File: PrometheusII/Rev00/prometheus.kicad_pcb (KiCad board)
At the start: 4 copper layers, 153.2 x 128.5 mm, 181 parts, among them J1 0878311420, J2 Conn_02x08_Odd_Even, Q1 MMBF4391, Q2 MMBF4391, Q3 BSS138, Q4 BSS84, Q5 BSS138, Q6 BSS84, U1 Teensy4.0_NoSD, U10 74LVC2G157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

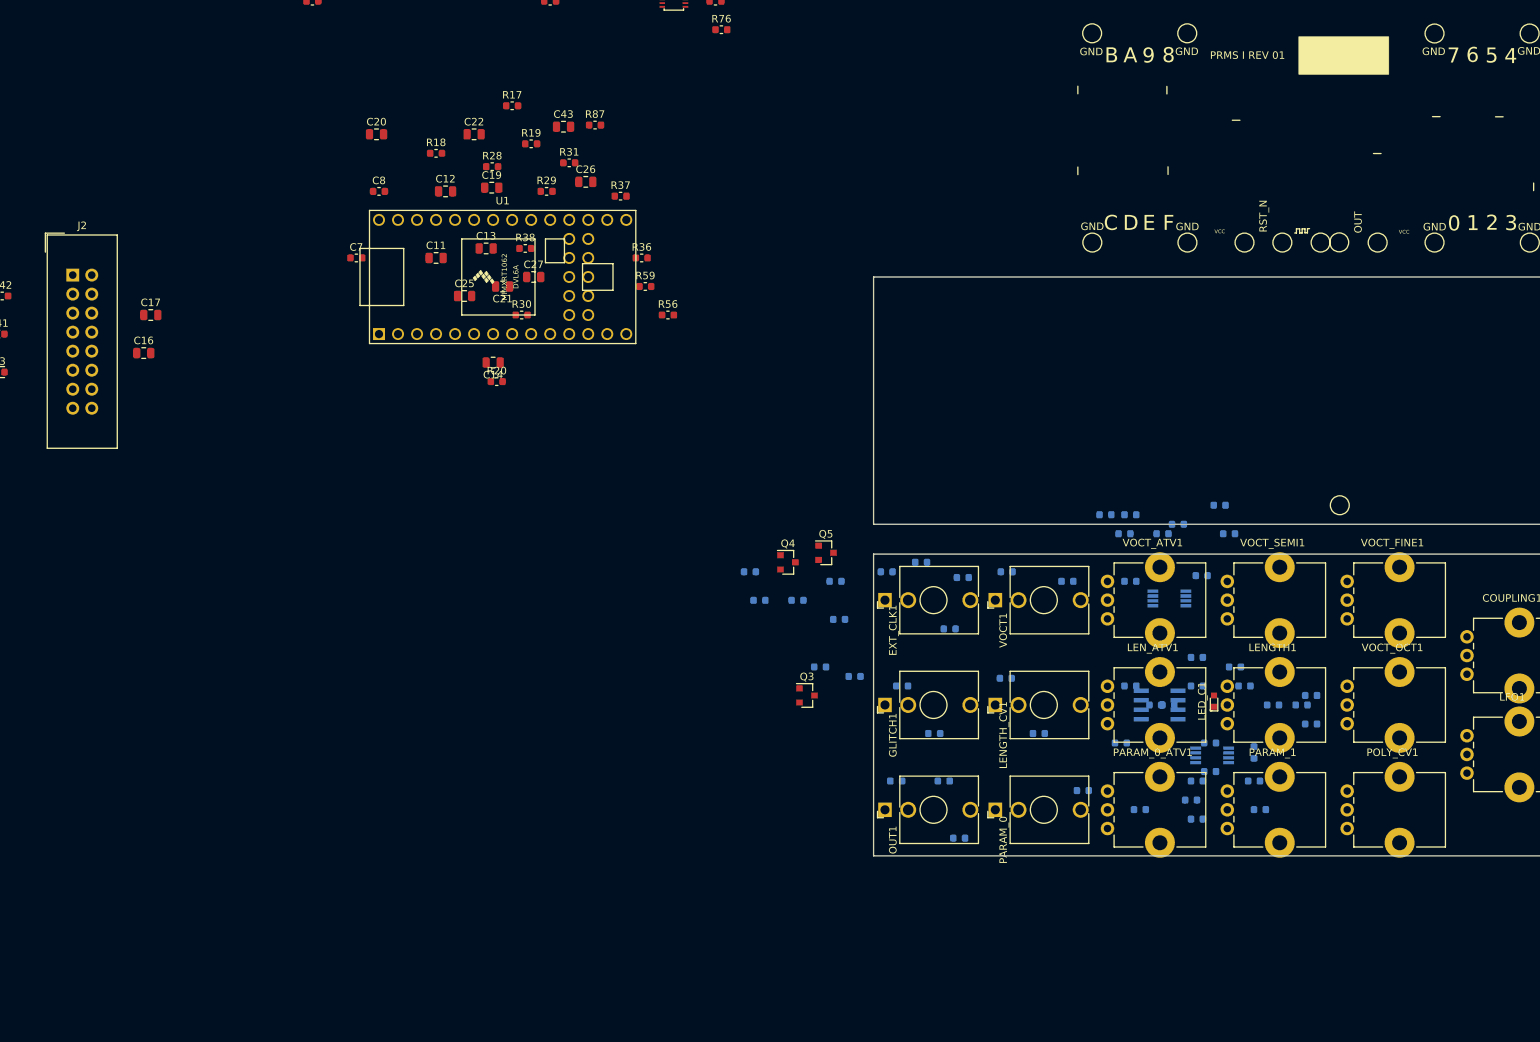
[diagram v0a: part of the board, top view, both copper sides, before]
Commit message: Updated panel layout
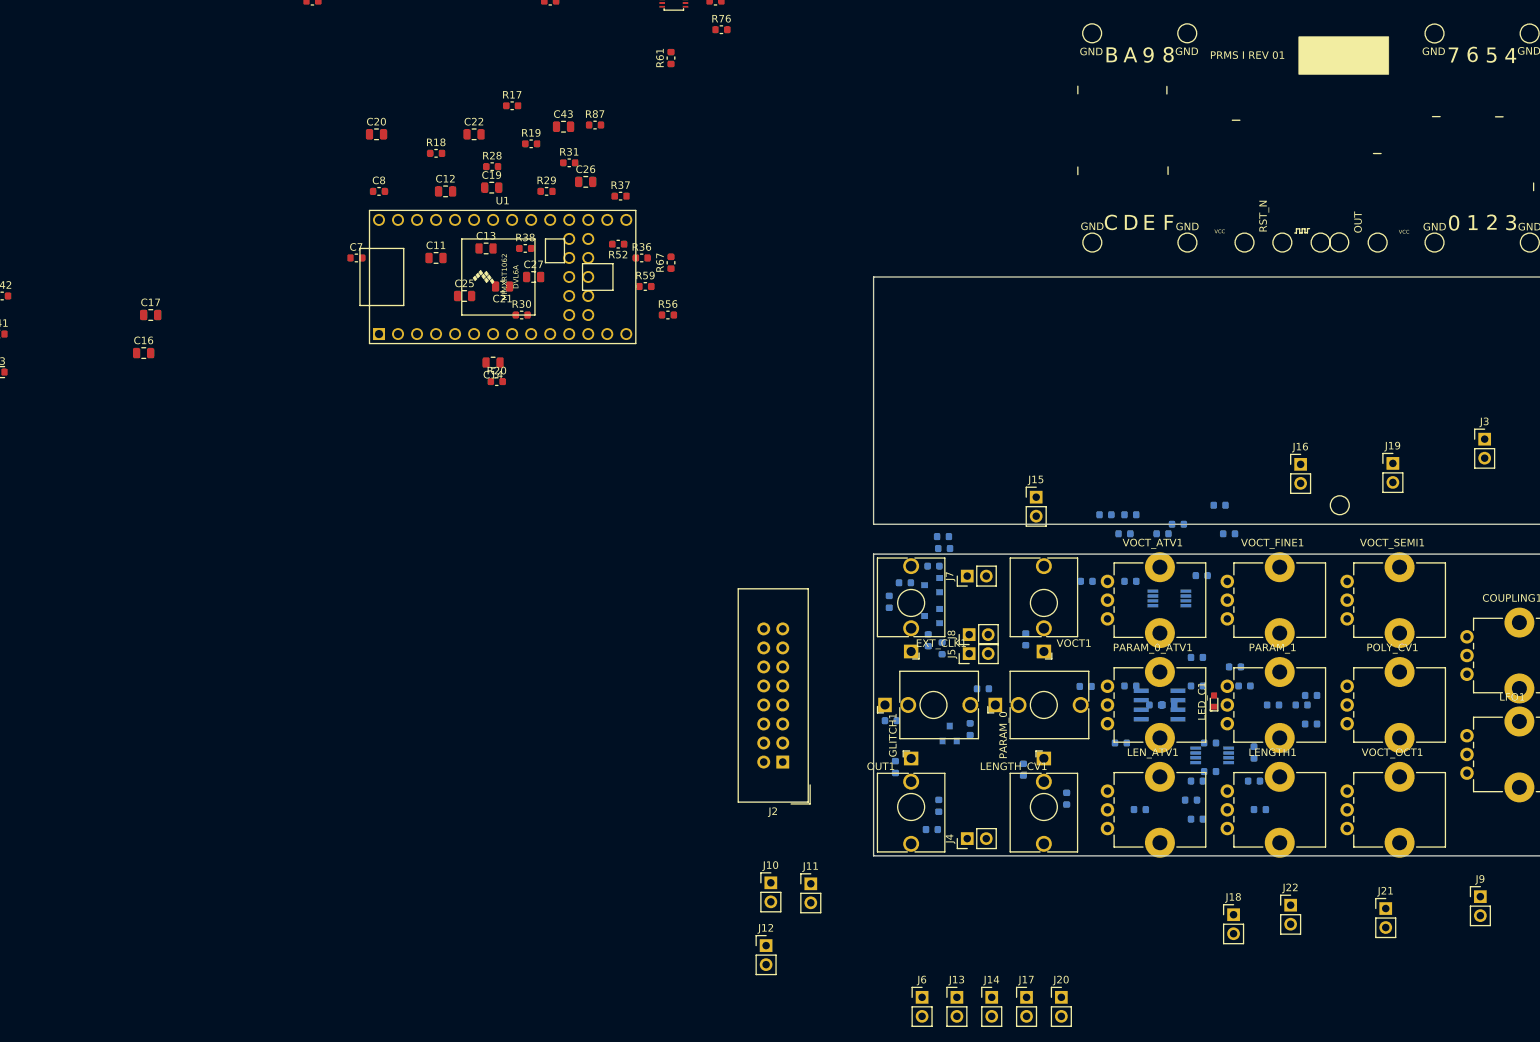
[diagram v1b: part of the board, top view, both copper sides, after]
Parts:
- added J10: Conn_02x01, Connector_PinHeader_2.54mm:PinHeader_1x02_P2.54mm_Vertical, F.Cu at (2.79, 133.0)
- added J11: Conn_02x01, Connector_PinHeader_2.54mm:PinHeader_1x02_P2.54mm_Vertical, F.Cu at (8.13, 133.1)
- added J12: Conn_02x01, Connector_PinHeader_2.54mm:PinHeader_1x02_P2.54mm_Vertical, F.Cu at (2.16, 141.4)
- added J13: Conn_02x01, Connector_PinHeader_2.54mm:PinHeader_1x02_P2.54mm_Vertical, F.Cu at (27.6, 148.3)
- added J14: Conn_02x01, Connector_PinHeader_2.54mm:PinHeader_1x02_P2.54mm_Vertical, F.Cu at (32.3, 148.3)
- added J15: Conn_02x01, Connector_PinHeader_2.54mm:PinHeader_1x02_P2.54mm_Vertical, F.Cu at (38.2, 81.5)
- added J16: Conn_02x01, Connector_PinHeader_2.54mm:PinHeader_1x02_P2.54mm_Vertical, F.Cu at (73.5, 77.1)
- added J17: Conn_02x01, Connector_PinHeader_2.54mm:PinHeader_1x02_P2.54mm_Vertical, F.Cu at (36.9, 148.3)
- added J18: Conn_02x01, Connector_PinHeader_2.54mm:PinHeader_1x02_P2.54mm_Vertical, F.Cu at (64.6, 137.2)
- added J19: Conn_02x01, Connector_PinHeader_2.54mm:PinHeader_1x02_P2.54mm_Vertical, F.Cu at (85.9, 77.0)
- added J20: Conn_02x01, Connector_PinHeader_2.54mm:PinHeader_1x02_P2.54mm_Vertical, F.Cu at (41.6, 148.3)
- added J21: Conn_02x01, Connector_PinHeader_2.54mm:PinHeader_1x02_P2.54mm_Vertical, F.Cu at (84.9, 136.4)
- added J22: Conn_02x01, Connector_PinHeader_2.54mm:PinHeader_1x02_P2.54mm_Vertical, F.Cu at (72.2, 136.0)
- added J3: Conn_02x01, Connector_PinHeader_2.54mm:PinHeader_1x02_P2.54mm_Vertical, F.Cu at (98.1, 73.7)
- added J4: Conn_02x01, Connector_PinHeader_2.54mm:PinHeader_1x02_P2.54mm_Vertical, F.Cu at (29.0, 127.1)
- added J5: Conn_02x01, Connector_PinHeader_2.54mm:PinHeader_1x02_P2.54mm_Vertical, F.Cu at (29.3, 102.4)
- added J6: Conn_02x01, Connector_PinHeader_2.54mm:PinHeader_1x02_P2.54mm_Vertical, F.Cu at (23.0, 148.3)
- added J7: Conn_02x01, Connector_PinHeader_2.54mm:PinHeader_1x02_P2.54mm_Vertical, F.Cu at (29.0, 92.0)
- added J8: Conn_02x01, Connector_PinHeader_2.54mm:PinHeader_1x02_P2.54mm_Vertical, F.Cu at (29.3, 99.8)
- added J9: Conn_02x01, Connector_PinHeader_2.54mm:PinHeader_1x02_P2.54mm_Vertical, F.Cu at (97.5, 134.8)
- Q3, Q4, Q5: moved to B.Cu
- R52, R61, R67: moved to F.Cu
- moved J2 115.0 mm to (4.38, 116.8), turned to 180 degrees
- moved R61 74.4 mm to (-10.5, 22.8), turned to 90 degrees
- moved R52 65.8 mm to (-17.6, 47.7), turned to 180 degrees
- moved R67 52.7 mm to (-10.5, 50.2), turned to 90 degrees
- moved R69 26.2 mm to (25.8, 86.7), turned to 180 degrees
- moved R68 25.6 mm to (25.9, 88.3), turned to 180 degrees
- moved R50 21.7 mm to (29.4, 112.5), turned to 90 degrees
- moved Q4 20.5 mm to (24.3, 97.3), turned to 180 degrees
- moved Q3 19.7 mm to (26.7, 113.0), turned to 90 degrees
- moved VOCT_FINE1 16.0 mm to (63.7, 97.7)
- moved VOCT_SEMI1 16.0 mm to (79.8, 97.7)
- moved Q5 14.8 mm to (24.3, 93.2), turned to 180 degrees
- moved LENGTH1 14.0 mm to (63.7, 125.7)
- moved LEN_ATV1 14.0 mm to (47.7, 125.7)
- moved PARAM_0 14.0 mm to (32.8, 109.2)
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
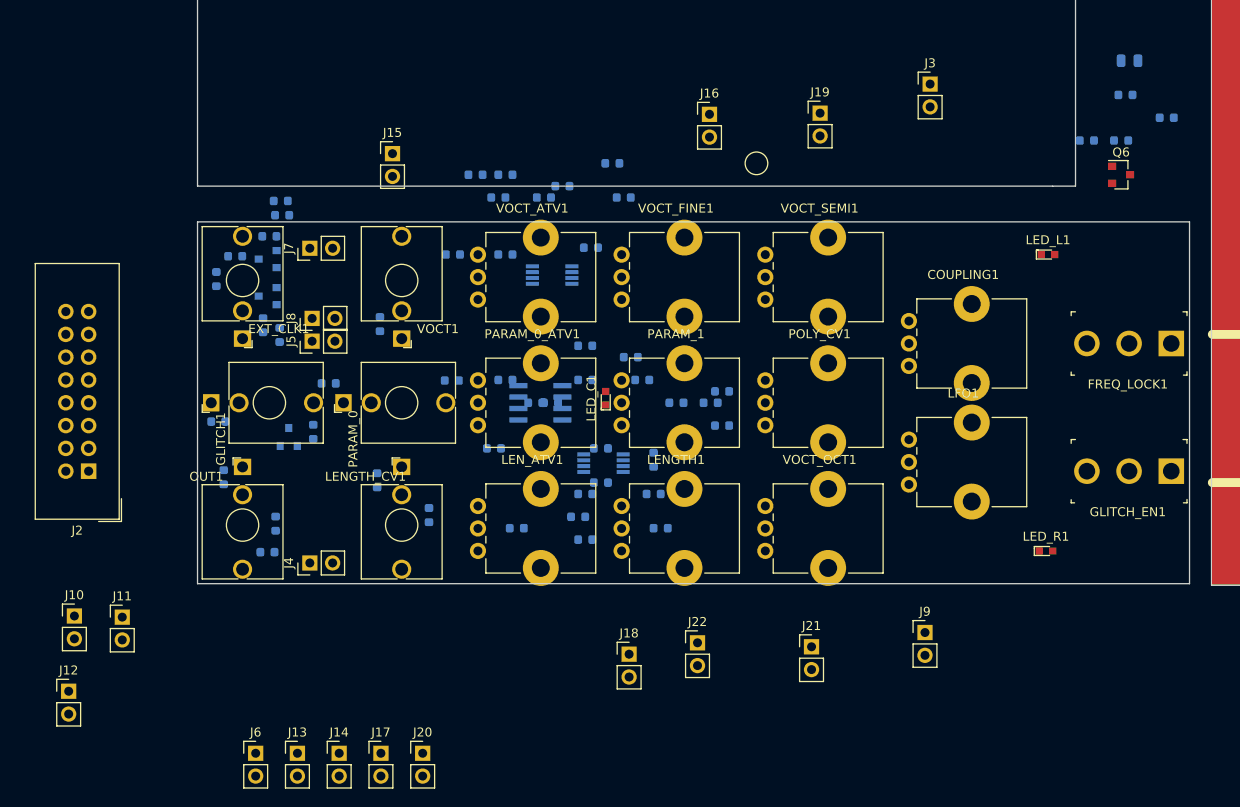
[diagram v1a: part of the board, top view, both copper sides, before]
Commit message: rough board to board connector placement
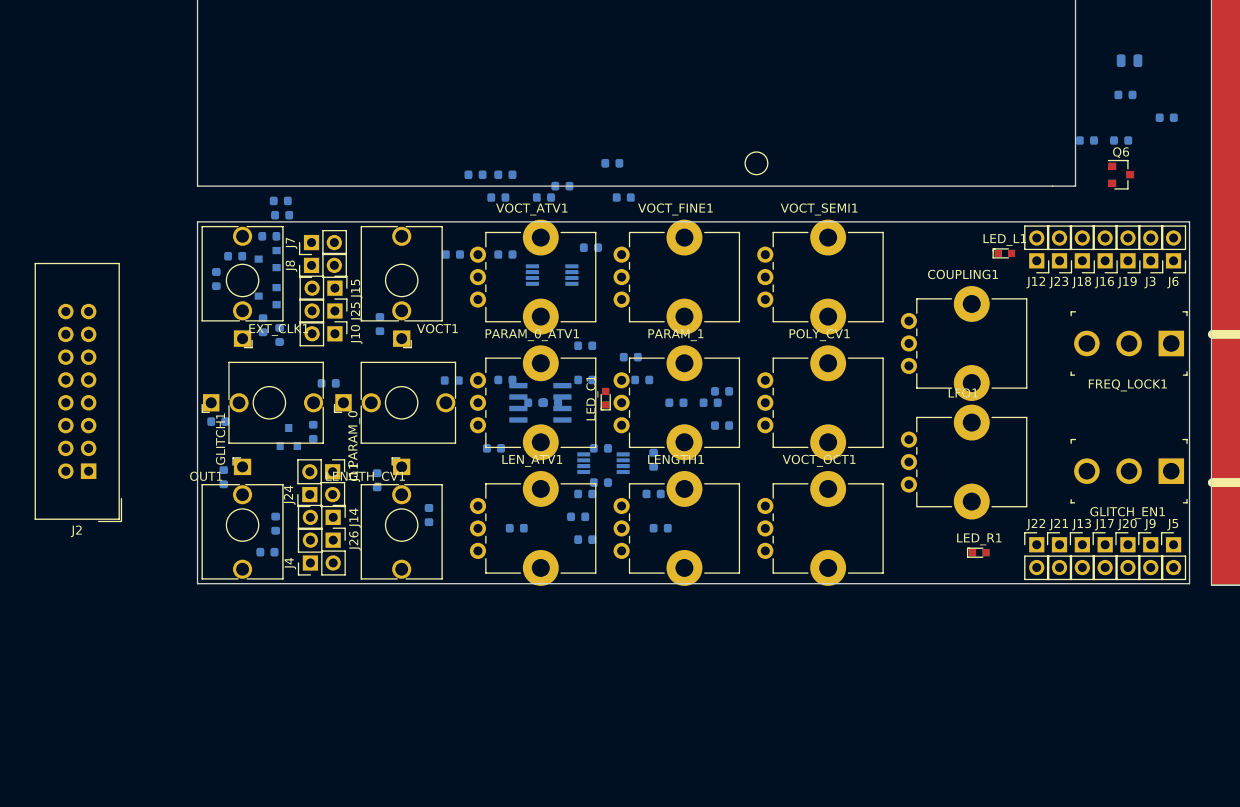
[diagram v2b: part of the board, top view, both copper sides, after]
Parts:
- added J23: Conn_02x01, Connector_PinHeader_2.54mm:PinHeader_1x02_P2.54mm_Vertical, F.Cu at (112.5, 93.4)
- added J24: Conn_02x01, Connector_PinHeader_2.54mm:PinHeader_1x02_P2.54mm_Vertical, F.Cu at (29.0, 119.4)
- added J25: Conn_02x01, Connector_PinHeader_2.54mm:PinHeader_1x02_P2.54mm_Vertical, F.Cu at (31.8, 99.0)
- added J26: Conn_02x01, Connector_PinHeader_2.54mm:PinHeader_1x02_P2.54mm_Vertical, F.Cu at (31.6, 124.5)
- moved J12 118.0 mm to (110.0, 93.4), turned to 180 degrees
- moved J6 116.0 mm to (125.2, 93.4), turned to 180 degrees
- moved J5 98.6 mm to (125.2, 125.0), turned to 0 degrees
- moved J13 90.5 mm to (115.1, 125.0)
- moved J17 83.9 mm to (117.6, 125.0)
- moved J20 81.9 mm to (120.1, 125.0)
- moved J18 66.8 mm to (115.1, 93.4), turned to 180 degrees
- moved J16 47.0 mm to (117.6, 93.4), turned to 180 degrees
- moved J10 42.8 mm to (31.8, 101.5), turned to 270 degrees
- moved J22 39.3 mm to (110.0, 125.0)
- moved J19 38.0 mm to (120.1, 93.4), turned to 180 degrees
- moved J3 31.5 mm to (122.7, 93.4), turned to 180 degrees
- moved J21 29.9 mm to (112.5, 125.0)
- moved J11 28.5 mm to (31.6, 116.9), turned to 270 degrees
- moved J9 27.0 mm to (122.7, 125.0)
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
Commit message: header unification
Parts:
- removed J10, J11, J14, J15, J24, J25, J26, J7, J8: Conn_02x01, Connector_PinHeader_2.54mm:PinHeader_1x02_P2.54mm_Vertical
- added C40: 1u, Capacitor_SMD:C_0603_1608Metric, F.Cu at (5.08, -2.54)
- added J3: Conn_02x05_Odd_Even, Connector_PinHeader_2.54mm:PinHeader_2x05_P2.54mm_Vertical, B.Cu at (31.8, 91.4)
- added J5: Conn_02x07_Odd_Even, Connector_PinHeader_2.54mm:PinHeader_2x07_P2.54mm_Vertical, F.Cu at (95.2, 82.5)
- added J6: Conn_02x07_Odd_Even, Connector_PinHeader_2.54mm:PinHeader_2x07_P2.54mm_Vertical, F.Cu at (109.2, 138.4)
- added R76: 0, Resistor_SMD:R_0603_1608Metric, F.Cu at (1.27, 5.08)
- added U10: 74LVC2G157, Package_SO:VSSOP-8_2.4x2.1mm_P0.5mm, F.Cu at (-2.54, 3.81)
- J4: value Conn_02x01 -> Conn_02x05_Odd_Even; footprint Connector_PinHeader_2.54mm:PinHeader_1x02_P2.54mm_Vertical -> Connector_PinHeader_2.54mm:PinHeader_2x05_P2.54mm_Vertical; moved to B.Cu
- moved J4 10.6 mm to (31.8, 116.8), turned to 180 degrees
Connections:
- J4 pad 1: /OUT -> +12V
- R68 pad 1: Net-(J7-Pad1) -> /EXT_CLK
- R69 pad 1: Net-(J7-Pad1) -> /EXT_CLK

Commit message: header deunification
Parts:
- removed J12, J13, J16, J17, J18, J19, J20, J21, J22, J23: Conn_02x01, Connector_PinHeader_2.54mm:PinHeader_1x02_P2.54mm_Vertical
- removed the J3 at (122.7, 93.4)
- removed the J5 at (95.2, 82.5)
- removed the J5 at (125.2, 125.0)
- removed the J6 at (109.2, 138.4)
- removed the J6 at (125.2, 93.4)
- added J5: Conn_02x04_Odd_Even, Connector_PinHeader_2.54mm:PinHeader_2x04_P2.54mm_Vertical, B.Cu at (102.9, 94.0)
- added J6: Conn_02x04_Odd_Even, Connector_PinHeader_2.54mm:PinHeader_2x04_P2.54mm_Vertical, B.Cu at (102.9, 127.0)
- added J8: Conn_02x03_Odd_Even, Connector_PinHeader_2.54mm:PinHeader_2x03_P2.54mm_Vertical, B.Cu at (124.5, 127.0)
- J9: value Conn_02x01 -> Conn_02x03_Odd_Even; footprint Connector_PinHeader_2.54mm:PinHeader_1x02_P2.54mm_Vertical -> Connector_PinHeader_2.54mm:PinHeader_2x03_P2.54mm_Vertical; moved to B.Cu
- moved J9 31.1 mm to (124.5, 94.0), turned to 90 degrees
- moved LED_R1 7.66 mm to (111.2, 125.7)
- moved LED_L1 4.81 mm to (111.2, 92.6)
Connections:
- J9 pad 1: /LFO -> Net-(J9-Pad1)

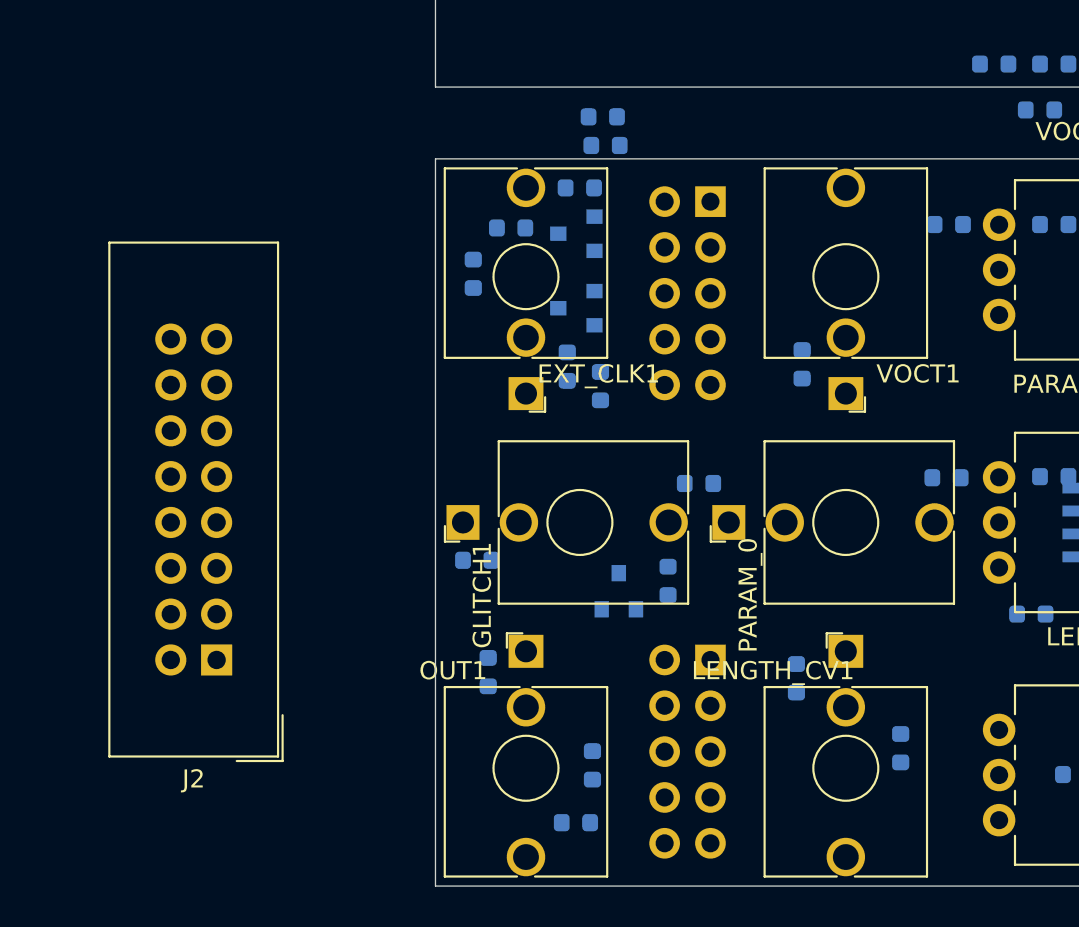
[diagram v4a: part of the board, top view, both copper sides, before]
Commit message: jack circuitry placement
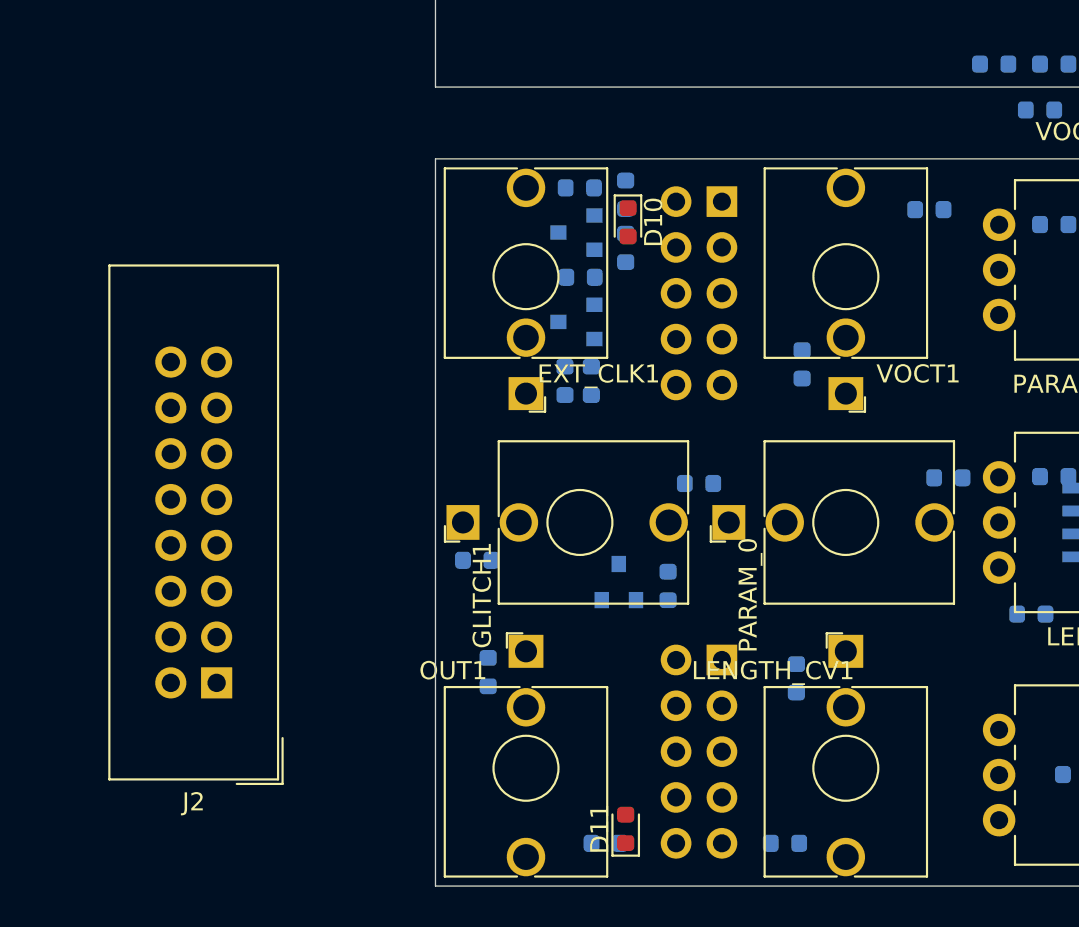
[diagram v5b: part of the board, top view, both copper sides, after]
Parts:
- D10, D11: moved to F.Cu
- moved D10 9.04 mm to (27.2, 92.6)
- moved D5 8.30 mm to (35.9, 127.0), turned to 180 degrees
- moved R68 5.79 mm to (27.1, 94.0), turned to 270 degrees
- moved R54 4.72 mm to (24.5, 95.6)
- moved R69 4.50 mm to (27.1, 91.1), turned to 90 degrees
- moved D11 3.97 mm to (27.1, 126.2)
- moved R51 2.01 mm to (25.9, 127.0), turned to 180 degrees
- moved D4 1.36 mm to (43.9, 91.9)
- moved J2 1.27 mm to (4.38, 118.1)
- moved R47 0.80 mm to (23.7, 101.4)
- moved Q4 0.76 mm to (24.3, 98.1)
- moved J3 0.63 mm to (32.4, 91.4)
- moved J4 0.63 mm to (32.4, 116.8)
- moved R49 0.59 mm to (25.1, 101.4)
- moved Q3 0.51 mm to (26.7, 112.5)
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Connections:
- J3 pad 2: /EXT_CLK_EN_T -> /EXT_CLK
- J3 pad 3: GND -> /VOCT_ATV
- J3 pad 4: /EXT_CLK -> GND
- J3 pad 5: /VOCT_ATV -> /VOCT_CV
- J3 pad 7: /VOCT_CV -> GND
- J3 pad 8: GND -> /EXT_CLK_EN_T
